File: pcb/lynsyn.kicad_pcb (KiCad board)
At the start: 4 copper layers, 72 x 52 mm, 78 parts, among them J1 USB Micro-B, J2 power_sensor, J3 Conn_ARM_JTAG_SWD_20, J4 Sync, J5 Cortex Debug, U1 EFM32GG332F1024, U10 74LVC2T45, U2 IP4220CZ6, U3 LMP8640, U4 LMP8640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

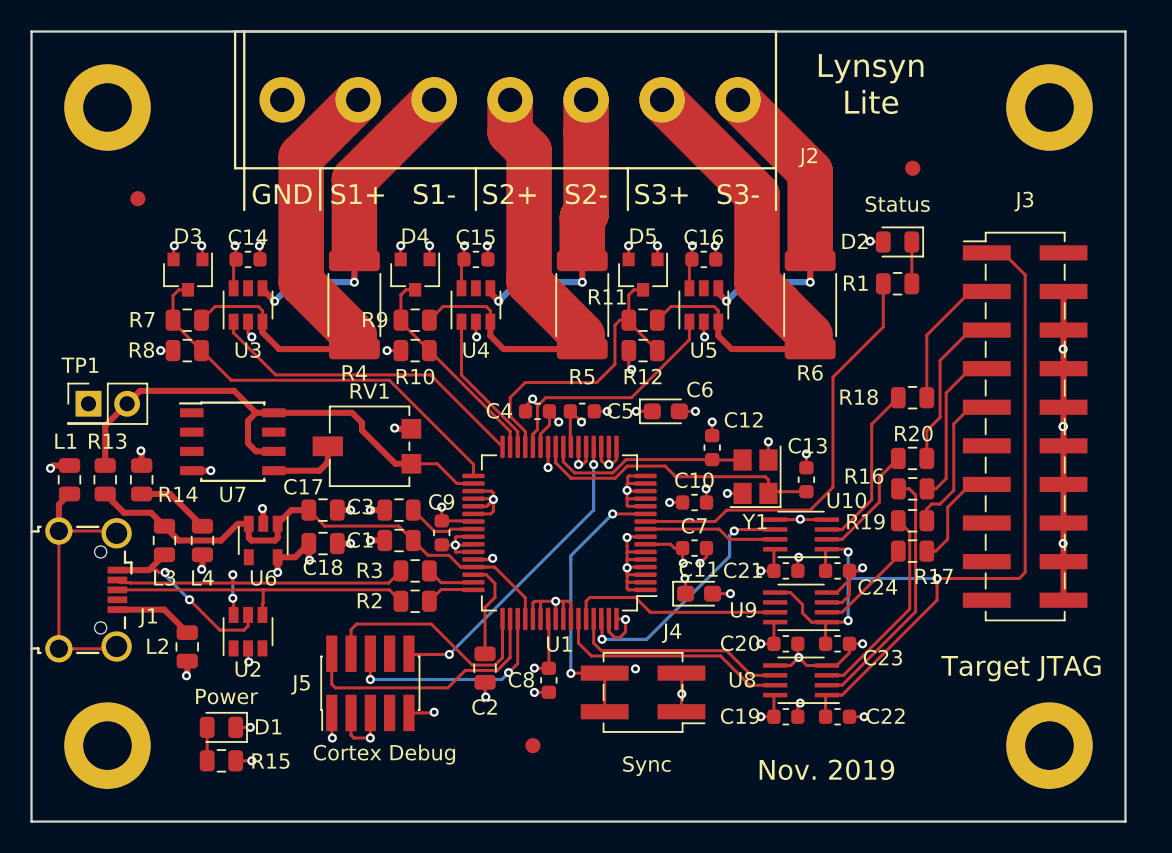
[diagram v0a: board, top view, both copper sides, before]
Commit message: Fixed silkscreen and added gerber files
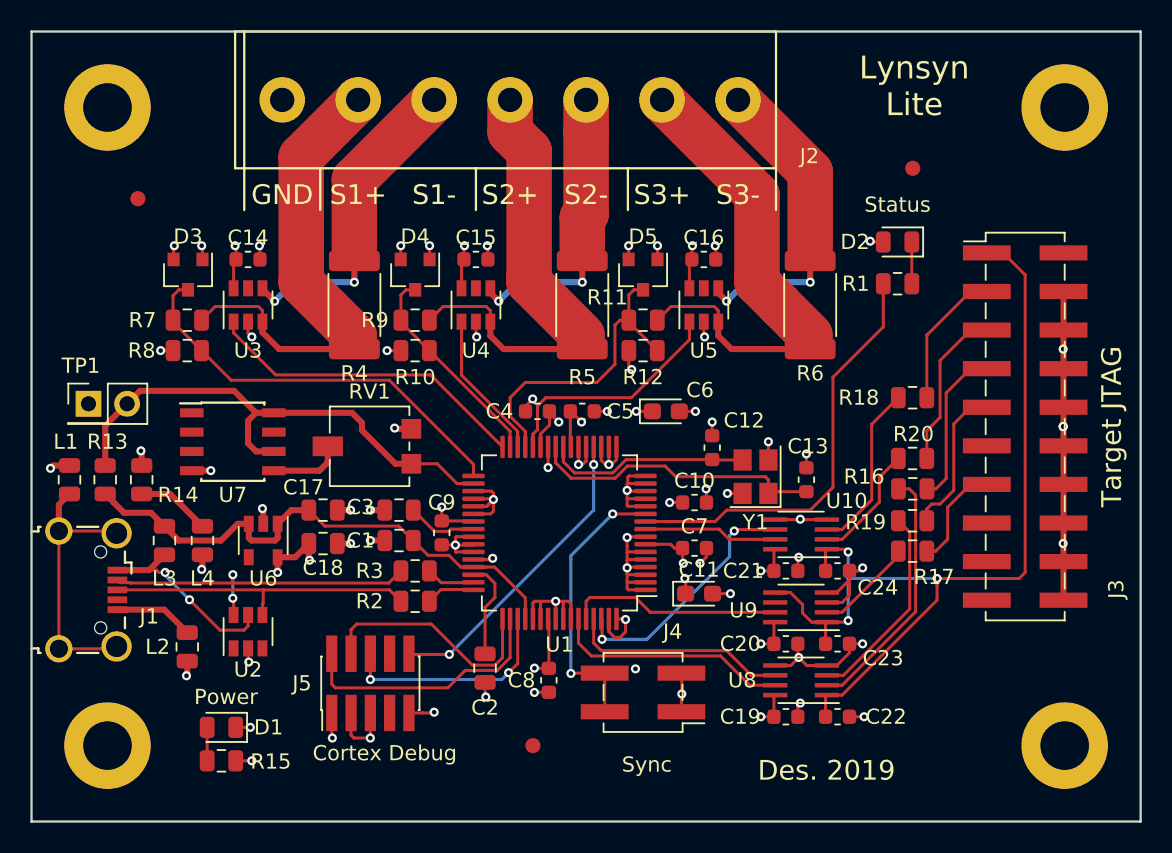
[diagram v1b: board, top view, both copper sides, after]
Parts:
- removed the REF** at (141.1, 141.2)
- removed the REF** at (141.1, 99.2)
- added REF**: MountingHole_3.2mm_M3_ISO7380_Pad, MountingHole:MountingHole_3.2mm_M3_ISO7380_Pad, F.Cu at (142.1, 141.2)
- added REF**: MountingHole_3.2mm_M3_ISO7380_Pad, MountingHole:MountingHole_3.2mm_M3_ISO7380_Pad, F.Cu at (142.1, 99.2)
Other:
- board size 72 x 52 mm -> 73 x 52 mm
- board text added: "Des. 2019"
- board text removed: "Nov. 2019"
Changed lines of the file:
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@@
-(kicad_pcb (version 20171130) (host pcbnew 5.0.0-fee4fd1~65~ubuntu17.10.1)
+(kicad_pcb (version 20171130) (host pcbnew 5.0.2-bee76a0~70~ubuntu18.04.1)
   (general
     (thickness 1.6)
@@
     (tags "Surface mounted pin header SMD 2x10 2.54mm double row")
     (attr smd)
-    (fp_text reference J3 (at 0 -14.9) (layer F.SilkS)
+    (fp_text reference J3 (at 6 10.7 90) (layer F.SilkS)
       (effects (font (size 1 1) (thickness 0.15)))
     )
@@
   )
   (module MountingHole:MountingHole_3.2mm_M3_ISO7380_Pad (layer F.Cu)
-    (at 141.065 141.19)
+    (at 142.065 141.19)
     (descr "Mounting Hole 3.2mm, M3, ISO7380")
     (tags "mounting hole 3.2mm m3 iso7380")
@@
   )
   (module MountingHole:MountingHole_3.2mm_M3_ISO7380_Pad (layer F.Cu)
-    (at 141.065 99.19)
+    (at 142.065 99.19)
     (descr "Mounting Hole 3.2mm, M3, ISO7380")
     (tags "mounting hole 3.2mm m3 iso7380")
@@
     )
   )
-  (gr_text "Nov. 2019" (at 126.389 142.831) (layer F.SilkS)
+  (gr_text "Des. 2019" (at 126.389 142.831) (layer F.SilkS)
     (effects (font (size 1.3 1.3) (thickness 0.2)))
   )
@@
     (effects (font (size 1 1) (thickness 0.15)))
   )
-  (gr_text "Target JTAG" (at 139.265 135.99) (layer F.SilkS)
+  (gr_text "Target JTAG" (at 145.165 120.19 90) (layer F.SilkS)
     (effects (font (size 1.3 1.3) (thickness 0.2)))
   )
-  (gr_text "Lynsyn\nLite" (at 129.315 97.69) (layer F.SilkS)
+  (gr_text "Lynsyn\nLite" (at 132.165 97.79) (layer F.SilkS)
     (effects (font (size 1.5 1.5) (thickness 0.3)))
   )
@@
     (effects (font (size 1.3 1.3) (thickness 0.2)))
   )
-  (gr_line (start 146.065 146.19) (end 74.065 146.19) (layer Edge.Cuts) (width 0.15))
-  (gr_line (start 146.065 94.19) (end 146.065 146.19) (layer Edge.Cuts) (width 0.15))
-  (gr_line (start 74.065 94.19) (end 146.065 94.19) (layer Edge.Cuts) (width 0.15))
+  (gr_line (start 147.065 146.19) (end 74.065 146.19) (layer Edge.Cuts) (width 0.15))
+  (gr_line (start 147.065 94.19) (end 147.065 146.19) (layer Edge.Cuts) (width 0.15))
+  (gr_line (start 74.065 94.19) (end 147.065 94.19) (layer Edge.Cuts) (width 0.15))
   (gr_line (start 74.065 146.19) (end 74.065 94.19) (layer Edge.Cuts) (width 0.15))
   (segment (start 101.4775 126.44) (end 101.115 126.0775) (width 0.2) (layer F.Cu) (net 1) (status 30))
@@
     (polygon
       (pts
-        (xy 74.565 94.69) (xy 74.565 145.69) (xy 142.565 145.69) (xy 142.565 94.69)
+        (xy 74.565 94.69) (xy 74.565 145.69) (xy 146.465 145.69) (xy 146.465 94.69)
       )
     )
@@
     (polygon
       (pts
-        (xy 126.565 94.69) (xy 142.565 94.69) (xy 142.565 145.69) (xy 74.565 145.69) (xy 74.565 124.69)
+        (xy 126.565 94.69) (xy 146.465 94.69) (xy 146.465 145.69) (xy 74.565 145.69) (xy 74.565 124.69)
         (xy 105.065 124.69) (xy 105.065 122.69) (xy 118.565 122.69) (xy 118.565 117.19) (xy 126.565 117.19)
       )
